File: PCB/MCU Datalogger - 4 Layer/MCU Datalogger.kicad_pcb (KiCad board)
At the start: 2 copper layers, 50.7 x 30.4 mm, 29 parts, among them J1 Conn_01x04_Pin, J2 Conn_01x04_Pin, J3 Conn_01x09_Pin, J4 Conn_02x03_Odd_Even, U1 24LC1025, U2 24LC1025, U3 DS1337S+, U4 ATMEGA328P-AU, Y1 16 MHz, Y2 32.768 Khz

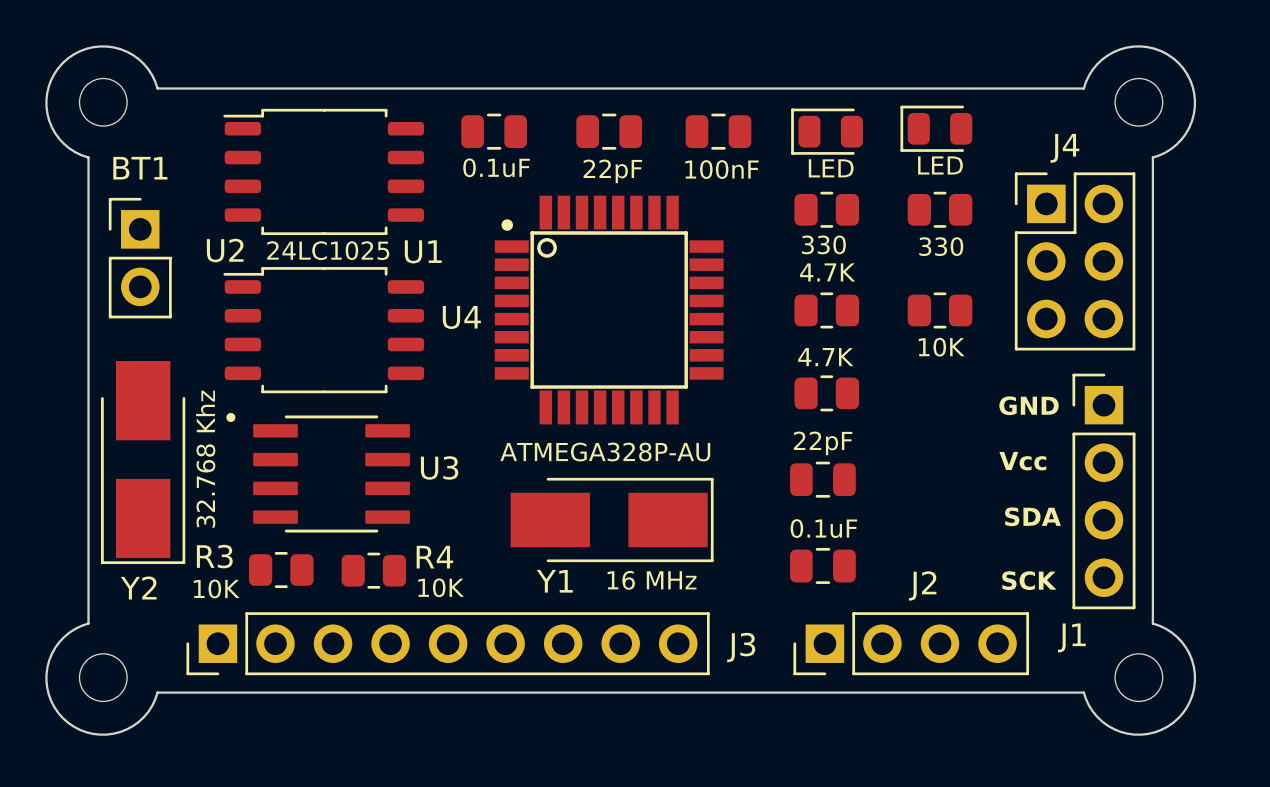
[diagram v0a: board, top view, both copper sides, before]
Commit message: 4-layer PCB routing
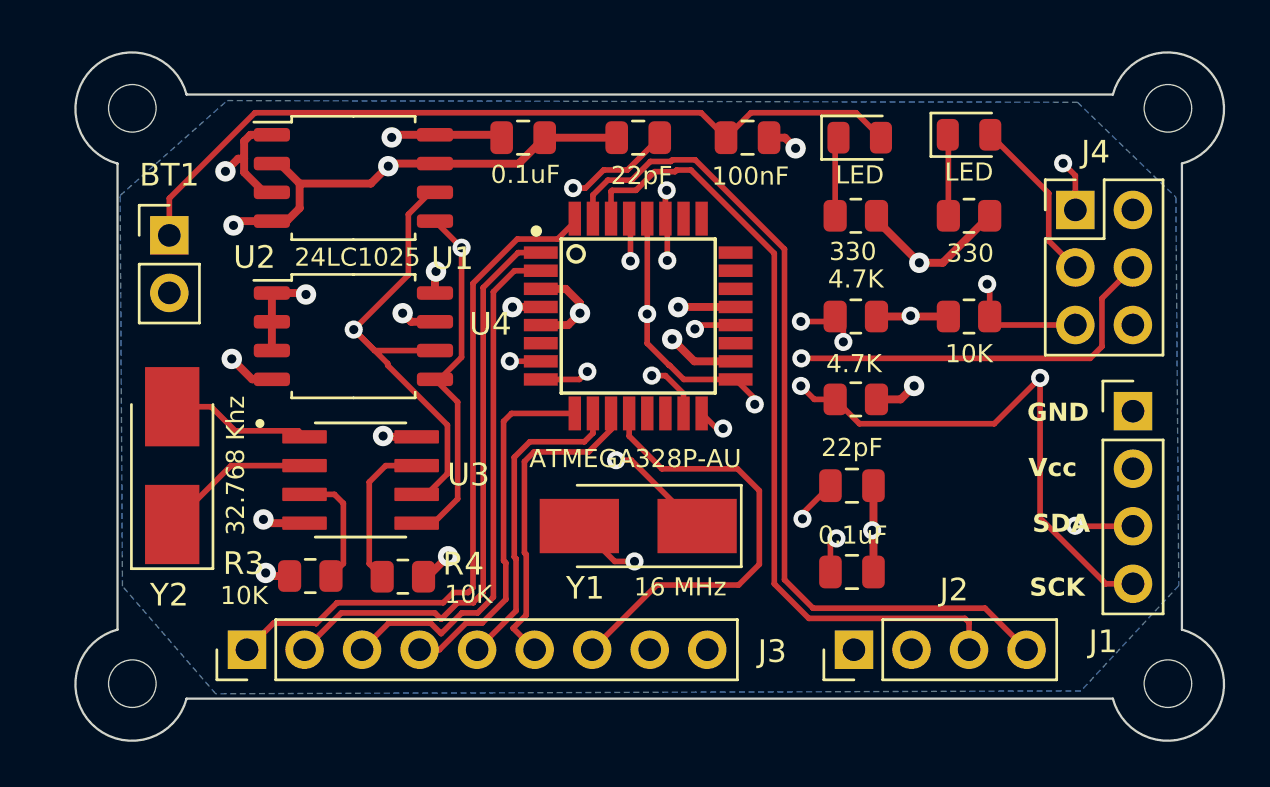
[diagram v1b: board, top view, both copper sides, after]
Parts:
- moved C4 1.31 mm to (144.4, 92.1)
- moved C5 1.31 mm to (154.3, 92.1)
- moved D1 1.31 mm to (159.3, 92.1)
- moved H4 1.31 mm to (172.9, 116.2)
- moved R1 1.31 mm to (159.1, 95.5)
- moved R2 1.31 mm to (164.1, 95.5)
- moved U3 1.31 mm to (137.2, 107.2)
- moved D2 1.31 mm to (164.1, 92.0)
- moved H3 1.31 mm to (172.9, 90.8)
- moved J1 1.31 mm to (171.3, 104.2)
- moved R3 1.31 mm to (135.0, 111.4)
- moved R4 1.31 mm to (139.1, 111.5)
- moved R5 1.31 mm to (159.1, 103.6)
- moved R6 1.31 mm to (159.1, 100.0)
- moved R7 1.31 mm to (164.1, 100.0)
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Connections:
- U4 pad 18: Net-(BT1-+) -> /Vcc
- U4 pad 4: Net-(BT1-+) -> /Vcc
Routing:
- net /SCK: track 0.00 -> 85.2 mm, vias 0 -> 5
- net /SDA: track 0.00 -> 55.9 mm, vias 0 -> 6
- net GND: track 0.00 -> 45.3 mm, vias 0 -> 10
- net /MISO: track 0.00 -> 44.6 mm, vias 0 -> 2
- net /TX: track 0.00 -> 38.3 mm
- net Net-(BT1-+): track 0.00 -> 36.0 mm
- net /RX: track 0.00 -> 35.4 mm
- net /D2: track 0.00 -> 30.3 mm
- net /Vcc: track 0.00 -> 29.0 mm, vias 0 -> 11
- net /MOSI: track 0.00 -> 27.1 mm, vias 0 -> 2
- net /D3: track 0.00 -> 25.8 mm
- net Net-(U4-PB6): track 0.00 -> 25.7 mm, vias 0 -> 3
- net Net-(U4-PB7): track 0.00 -> 24.9 mm, vias 0 -> 3
- net /RESET: track 0.00 -> 24.1 mm, vias 0 -> 2
- net /D4: track 0.00 -> 23.1 mm
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- added copper zone on In2.Cu, net /Vcc
- added copper zone on B.Cu, net GND
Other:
- copper layers 2 -> 4
